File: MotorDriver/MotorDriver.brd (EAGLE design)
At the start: 50 x 50 mm, 85 parts, among them IC1 DRV8320RSRHAR, IC2 MAX3051ESA+, IC3 TPD4S014DSQR, J1 J_USB_MICROAB_HIROSE_ZX62-AB-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, J2 SM03B-ZESS-TB, Q1 BUK7Y7R8-80EX, Q2 BUK7Y7R8-80EX, Q3 BUK7Y7R8-80EX, Q4 BUK7Y7R8-80EX, Q5 BUK7Y7R8-80EX, Q6 BUK7Y7R8-80EX, U1 LPC1549JBD48, U2 ADCMP350YKSZ, U3 MCP1700T-33, U4 ADR5041, Y1 FA238V

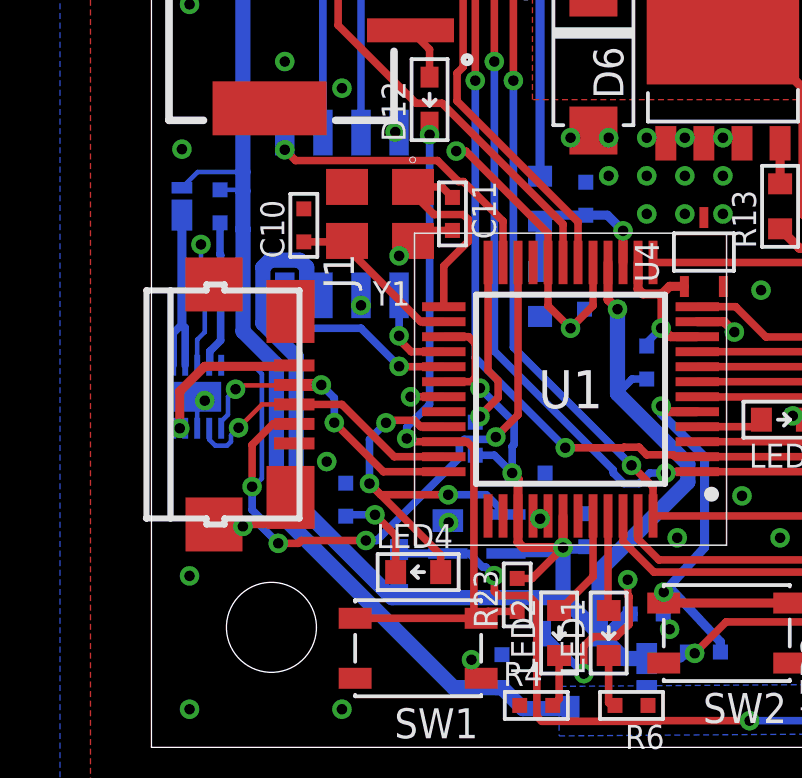
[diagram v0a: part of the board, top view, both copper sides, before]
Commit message: デバイス側で`id`を使ってUSBの接続を検出するのは不可能なので保護ICの`!ack`を使うように変更
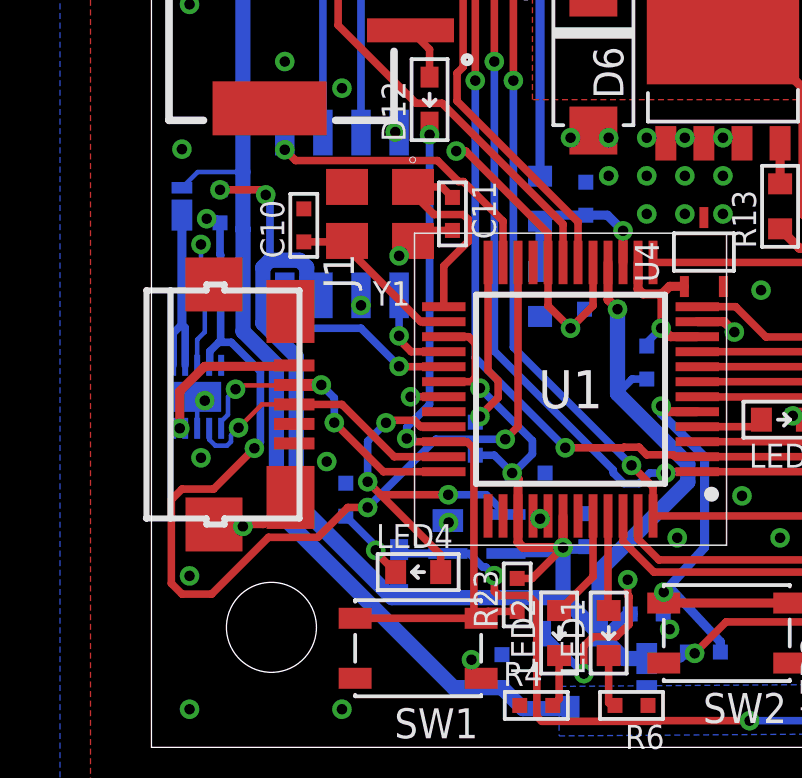
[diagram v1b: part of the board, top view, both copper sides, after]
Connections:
- removed net ID: IC3.5, J1.P$4, U1.22
- removed net N$29: IC3.4, R12.1
- new net !USB_ACK: IC3.4, R12.1, U1.22
- net +3V3: now also R12.2
- net +5V: no longer R12.2
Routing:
- net !USB_ACK: track 0.00 -> 35.6 mm, vias 0 -> 4
- net ID: track 25.9 -> 0.00 mm, vias 4 -> 0
- net N$29: track 4.92 -> 0.00 mm
- net +3V3: track 69.4 -> 73.8 mm, vias 5 -> 7
- net +5V: track 91.0 -> 90.3 mm
- net N$27: track 3.19 -> 2.55 mm
- net GND: vias 78 -> 79

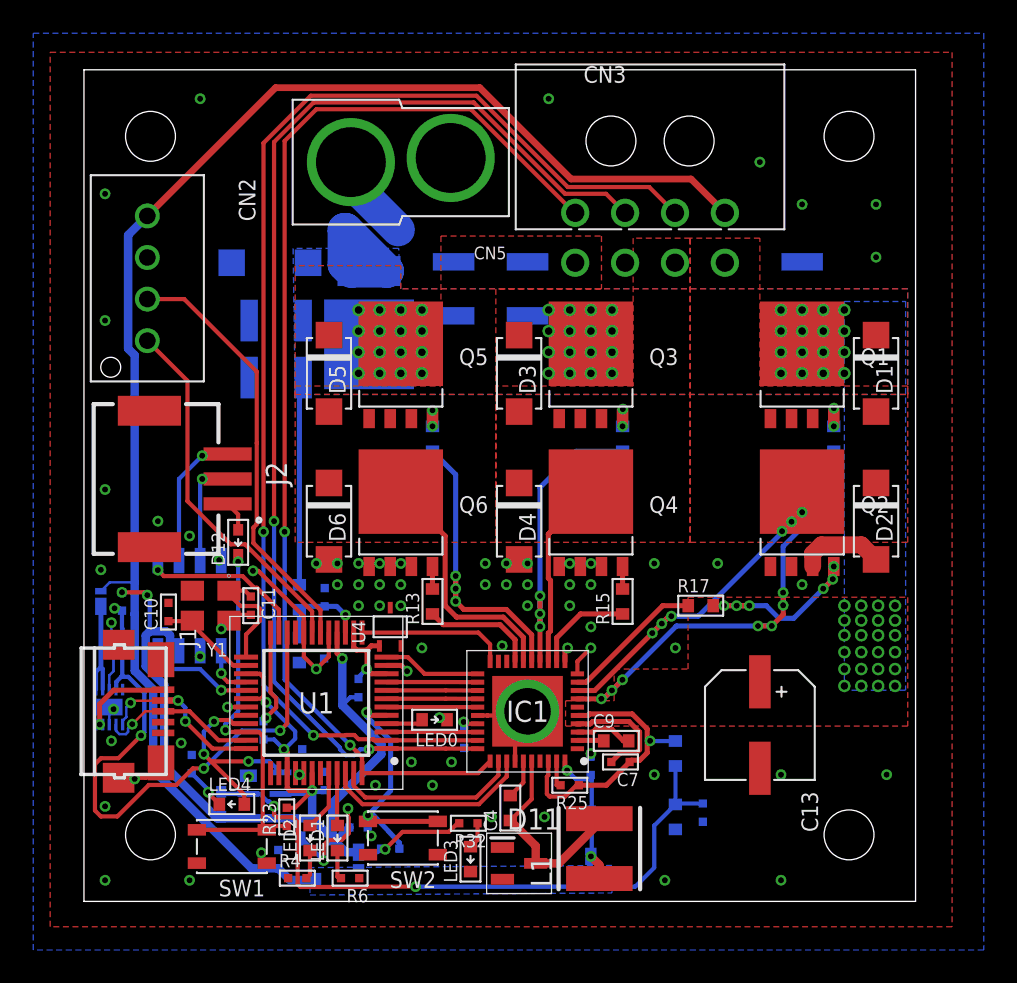
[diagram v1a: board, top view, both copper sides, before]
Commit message: [fix]USB-ACKのプルアップ抵抗の変更とコメントの整理
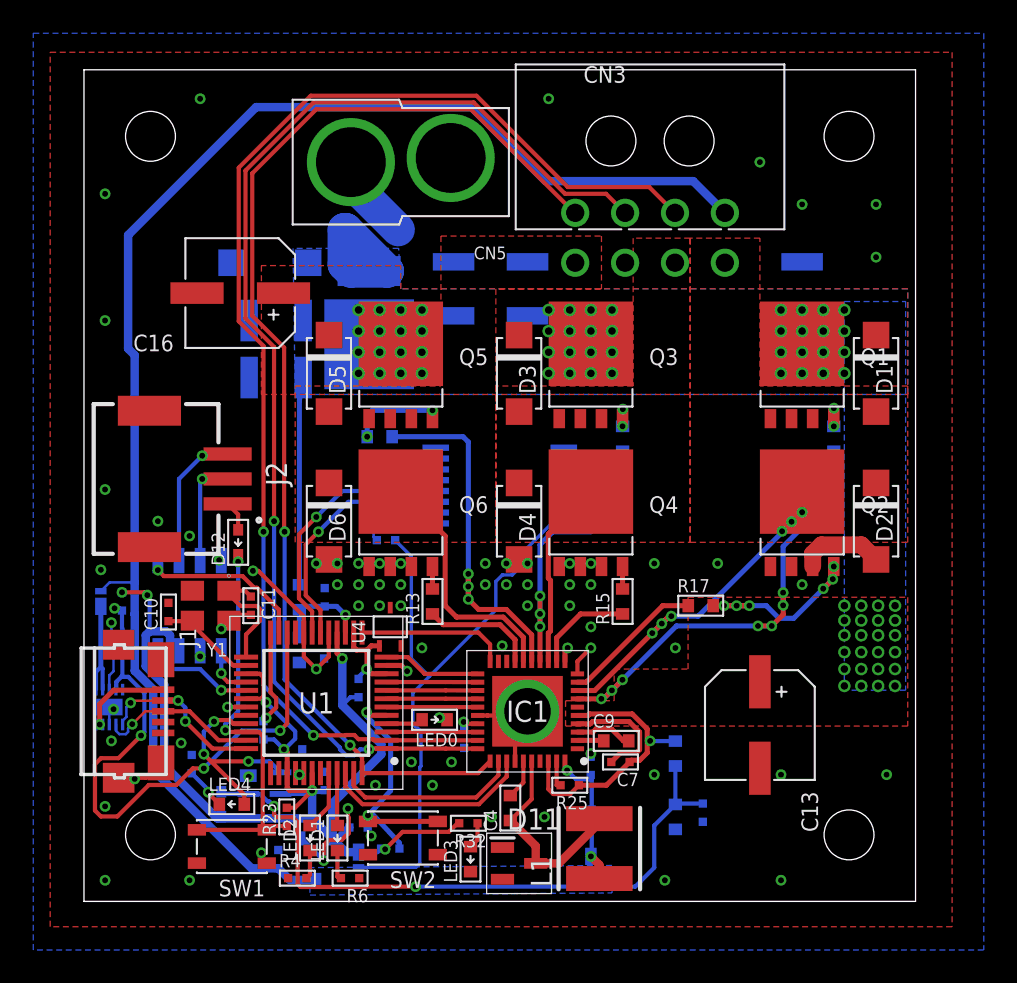
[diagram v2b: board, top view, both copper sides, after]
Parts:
- removed CN2: (no value), con-Molex:53375-04
- added C15: 0.1u, MotorDriver:C1005
- added C16: 22u, Passive:ES-6.3
- added LED5: RED, MotorDriver:LED1608
- added R8: 4.7k, MotorDriver:R1005
- added U5: AS5145B, ic-ams:SSOP16
- D10: value SMAJ60A -> SMAJ54A
- F1: value 15 -> 20
- LED0, LED3: value (none) -> RED
- LED1: value (none) -> GREEN
- LED2: value (none) -> WHITE
- R12: value 2.2k -> 10k
- R18: value (none) -> 10k
- moved R3 3.18 mm to (17.8, 27.9), turned to 0 degrees
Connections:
- new net N$29: C15.1, U5.15
- new net N$30: LED5.K, U5.1, U5.2
- new net N$32: LED5.A, R8.1
- net +5V: now also R8.2, U5.16; no longer CN2.4
- net GND: now also C15.2, C16.N, U5.10, U5.11, U5.7, U5.8; no longer CN2.3
- net QEI_A: now also U5.3; no longer CN2.2
- net QEI_B: now also U5.4; no longer CN2.1
- net V+: now also C16.P
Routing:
- net +5V: track 90.3 -> 127.4 mm
- net QEI_A: track 25.8 -> 14.5 mm, vias 0 -> 1
- net QEI_B: track 22.2 -> 15.5 mm, vias 0 -> 1
- net N$13: track 1.47 -> 5.84 mm
- net GH_C: track 18.1 -> 22.0 mm
- net N$29: track 0.00 -> 3.07 mm
- net N$30: track 0.00 -> 3.00 mm
- net HALL_W: track 68.8 -> 70.4 mm
- net HALL_V: track 71.6 -> 73.0 mm
- net N$32: track 0.00 -> 1.35 mm
- net HALL_U: track 75.7 -> 76.9 mm

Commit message: [fix]仕様確定に伴って変更
*電源電圧を24[V]に
*エンコーダICが廃盤になったので変更
*電源強化
*部品票の更新
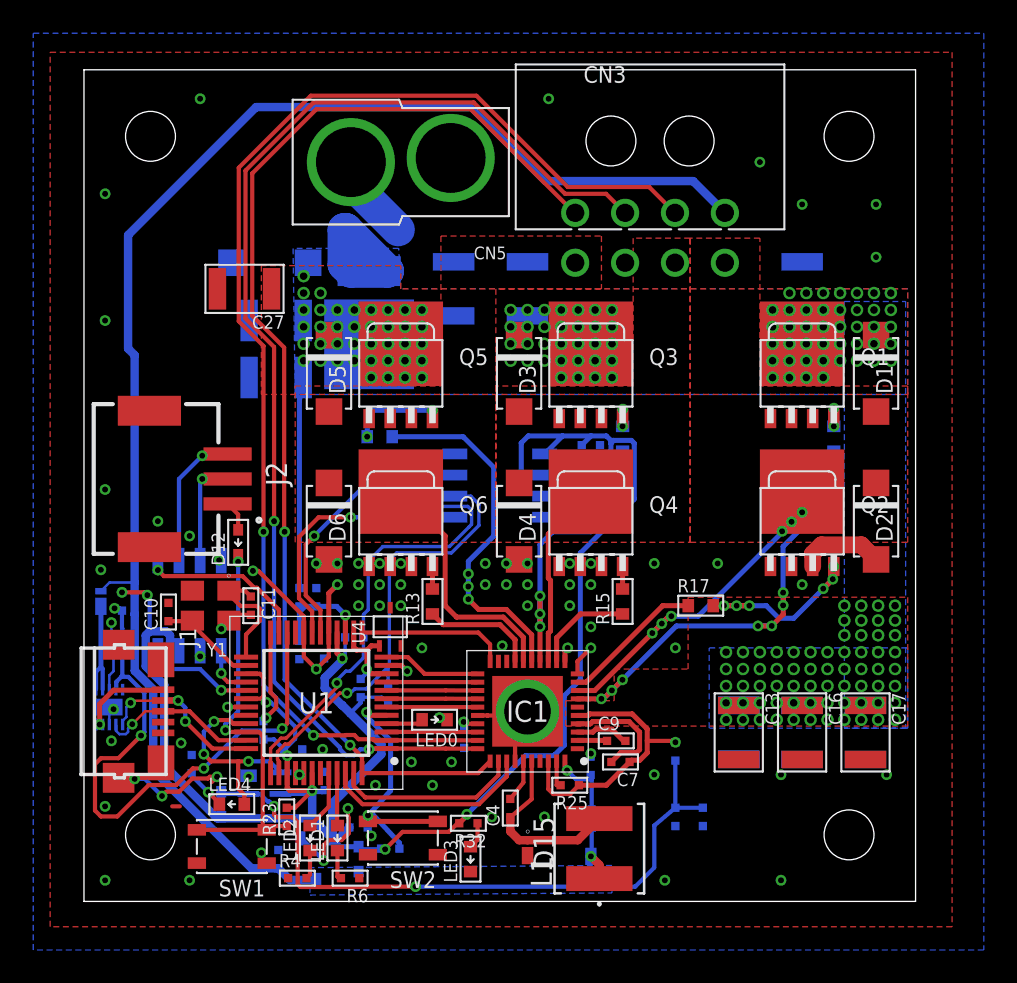
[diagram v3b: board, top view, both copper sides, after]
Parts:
- removed D11: HSMS-2800-TR1G, HSMS-2800-TR1G:SOT96P240X120-3N
- removed LED5: RED, MotorDriver:LED1608
- removed R8: 4.7k, MotorDriver:R1005
- removed U5: AS5145B, ic-ams:SSOP16
- added C17, C18, C21, C25, C26, C27: 10u, MotorDriver:C3225
- added C28: 0.1u, MotorDriver:C1005
- added D15: SDM2U40CSP-7B, SDM2U40CSP-7B:X3-WLB1608-2
- added IC5: AS5601-ASOM, AS5601-ASOM:SOIC127P600X175-8N
- added R19, R24: 2.2k, MotorDriver:R1005
- C1, C2, C3: value 10u -> 22u
- C13, C16: value 22u -> 10u; device Passive:ES-6.3 -> MotorDriver:C3225
- C14, C5: value 0.47u -> 47n
- C4, C9: device MotorDriver:C1608 -> MotorDriver:C1005
- CN3: device con-Molex:43045-0800 -> MotorDriver:43045-0800
- D1, D2, D3, D4, D5, D6: value NRVTSA4100ET3G -> SK34ATR
- D10: value SMAJ54A -> SMAJP4KE30A
- D13: device Diode:SMPC -> diode:SMPC
- D7: value SDM2U40CSP-7B -> (none); device SDM2U40CSP-7B:X3-WLB1608-2 -> MotorDriver:DIODE_SOD523
- L1: value NR5040T330M -> NR5040T2R2N; device NR5040T330M:NR5040T2R2N -> nr5040:IND_TAIYO_NR5040
- LED4: value (none) -> RED
- Q1, Q2, Q3, Q4, Q5, Q6: value BUK7Y7R8-80EX -> BUK7Y3R5-40E; device MotorDriver:SOT669 -> NXP_60_26022015:SOT669
- R10, R22, R9: device MotorDriver:R1608 -> MotorDriver:R1005
- R20: value 47k -> 22k; device MotorDriver:R1608 -> MotorDriver:R1005
- moved C16 42.9 mm to (43.2, 10.2), turned to 270 degrees
- moved C13 1.35 mm to (39.4, 10.2)
- moved C5 0.51 mm to (14.0, 18.3)
- moved C15 0.36 mm to (30.5, 25.7), turned to 0 degrees
- moved C14 0.25 mm to (37.2, 5.08)
- moved D7 0.13 mm to (16.5, 2.54)
- moved R21 0.13 mm to (16.6, 12.8)
- moved R9 0.13 mm to (35.6, 9.02)
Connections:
- removed net N$29: C15.1, U5.15
- removed net N$30: LED5.K, U5.1, U5.2
- removed net N$32: LED5.A, R8.1
- new net SCL: IC5.7, R19.1, U1.37
- new net SDA: IC5.6, R24.1, U1.38
- net +3V3: now also C15.1, C28.1, D7.A, IC5.1, IC5.2, R19.2, R24.2; no longer D7.2
- net +5V: now also D7.K; no longer D7.1, R8.2, U5.16
- net GND: now also C13.2, C16.2, C17.2, C18.2, C21.2, C25.2, C26.2, C27.2, C28.2, D15.2, IC5.4; no longer C13.N, C16.N, D11.1, U5.10, U5.11, U5.7, U5.8
- net N$3: now also D15.1; no longer D11.3
- net QEI_A: now also IC5.8; no longer U5.3
- net QEI_B: now also IC5.5; no longer U5.4
- net V+: now also C13.1, C16.1, C17.1, C18.1, C21.1, C25.1, C26.1, C27.1; no longer C13.P, C16.P
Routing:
- net +3V3: track 73.8 -> 121.3 mm, vias 7 -> 8
- net +5V: track 127.4 -> 89.3 mm
- net SCL: track 0.00 -> 28.3 mm, vias 0 -> 1
- net SDA: track 0.00 -> 26.8 mm, vias 0 -> 1
- net GND: track 39.4 -> 49.3 mm, vias 79 -> 82
- net N$29: track 3.07 -> 0.00 mm
- net N$30: track 3.00 -> 0.00 mm
- net QEI_A: track 14.5 -> 16.9 mm
- net N$32: track 1.35 -> 0.00 mm
- net N$3: track 12.5 -> 11.2 mm
- net FUSE: track 12.7 -> 12.1 mm
- net V+: track 29.0 -> 29.2 mm, vias 73 -> 182

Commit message: tmpからもってきた
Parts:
- removed D14: RB520S, MotorDriver:DIODE_SOD523
- removed D15: SDM2U40CSP-7B, SDM2U40CSP-7B:X3-WLB1608-2
- removed IC1: DRV8320RSRHAR, DRV8320RSRHAR:QFN50P600X600X100-41N
- removed LED4: RED, MotorDriver:LED1608
- removed R10: 2.2k, MotorDriver:R1005
- removed R11: 330, MotorDriver:R1005
- removed R9: 33k, MotorDriver:R1005
- removed U2: ADCMP350YKSZ, adcmp350:KS_4
- added C29, C31: 1u, MotorDriver:C1005
- added C30: 47n, MotorDriver:C1005
- added IC4: DRV8320SRTVT, DRV8320SRTVT:QFN50P500X500X80-33N
- added IC6: LM5160QPWPRQ1, LM5160QPWPRQ1:SOP65P640X110-15N
- added R27: 2.2k, MotorDriver:R1005
- added R28: 2.2, MotorDriver:R1005
- added R8: 51k, MotorDriver:R1005
- C14: value 47n -> 10u; device MotorDriver:C1005 -> MotorDriver:C3225
- C4: value 0.1u -> 10n
- C7: value 1u -> 0.1u
- C8: value 1u -> 4.7u; device MotorDriver:C1005 -> Passive:1608
- C9: value 47n -> 22n
- L1: value NR5040T2R2N -> 15u; device nr5040:IND_TAIYO_NR5040 -> Passive:L4949
- R1: value 12k -> 120k
- R2: value 2.2k -> 10k
- R25: value 100k -> 3.3k
- moved R1 43.8 mm to (9.02, 43.2)
- moved C9 39.5 mm to (7.75, 40.8), flipped to the bottom, turned to 90 degrees
- moved R2 39.0 mm to (9.02, 40.8)
- moved L1 37.7 mm to (3.68, 29.2), flipped to the bottom, turned to 270 degrees
- moved C7 35.3 mm to (7.62, 33.7), flipped to the bottom, turned to 270 degrees
- moved D8 34.6 mm to (3.68, 24.3), turned to 180 degrees
- moved R25 31.9 mm to (8.38, 31.1), flipped to the bottom, turned to 90 degrees
- moved C4 31.5 mm to (7.11, 31.1), flipped to the bottom
- moved C8 23.5 mm to (2.03, 20.6), turned to 90 degrees
- moved C14 5.27 mm to (35.8, 10.2), flipped to the top, turned to 270 degrees
- moved C18 3.56 mm to (35.8, 10.2)
- moved U4 0.57 mm to (18.7, 17.0)
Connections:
- removed net FUSE: LED4.A, U1.33, U2.3
- removed net N$20: IC1.39, R25.2
- removed net N$25: C14.2, D14.A, R10.2, R9.1, U2.1
- removed net N$27: LED4.K, R11.2
- new net N$32: C31.1, IC4.24
- new net N$48: C30.1, IC4.32
- new net N$55: C29.2, IC4.2
- new net N$56: C30.2, IC4.1
- new net VBAT/2: CN5.P, F1.2, IC6.3, R1.2, R8.1
- net !BRAKE: now also IC4.30; no longer IC1.33
- net !CS: now also IC4.21; no longer IC1.24
- net !FAULT: now also IC4.17; no longer IC1.20
- net +3V3: no longer D14.K, U2.4
- net DIR: now also IC4.29; no longer IC1.32
- net GH_A: now also IC4.5; no longer IC1.7
- net GH_B: now also IC4.12; no longer IC1.14
- net GH_C: now also IC4.13; no longer IC1.15
- net GL_A: now also IC4.7; no longer IC1.9
- net GL_B: now also IC4.10; no longer IC1.12
- net GL_C: now also IC4.15; no longer IC1.17
- net GND: now also C14.2, C31.2, C7.1, C8.1, C9.1, IC4.16, IC4.23, IC4.31, IC4.33, IC4.8, IC4.9, IC6.1, IC6.15, IC6.2, R2.1, R27.2; no longer C14.1, C8.2, D15.2, IC1.1, IC1.10, IC1.11, IC1.18, IC1.19, IC1.26, IC1.34, IC1.41, R10.1, R11.1, R2.2, U2.2
- net HALL_U: now also IC4.26; no longer IC1.29
- net HALL_V: now also IC4.27; no longer IC1.30
- net HALL_W: now also IC4.28; no longer IC1.31
- net N$1: now also C7.2, IC6.10, IC6.8; no longer IC1.40, R1.2, R2.1
- net N$16: now also C4.1, IC6.12, IC6.13, L1.1; no longer C7.2, IC1.4
- net N$17: now also IC6.9, R25.2, R27.1; no longer C8.1, IC1.27
- net N$18: now also C4.2, IC6.11; no longer C9.1, IC1.2
- net N$19: now also C8.2, R28.2; no longer C9.2, IC1.3
- net N$2: now also IC6.5, R8.2; no longer D8.2, L1.1, R1.1
- net N$26: now also D8.2, L1.2, R25.1, R28.1; no longer CN5.P, F1.2
- net N$3: now also IC6.4, R1.1, R2.2; no longer C4.1, D15.1, IC1.36, L1.2
- net N$4: now also C9.2, IC6.6; no longer C4.2, IC1.35
- net PWM_AH: now also IC4.25; no longer IC1.28
- net PWM_EN: now also IC4.22; no longer IC1.25
- net SCLK: now also IC4.20; no longer IC1.23
- net SDI: now also IC4.19; no longer IC1.22
- net SDO: now also IC4.18; no longer IC1.21
- net SH_A: now also IC4.6; no longer IC1.8
- net SH_B: now also IC4.11; no longer IC1.13
- net SH_C: now also IC4.14; no longer IC1.16
- net V+: now also C14.1, C29.1, IC4.3, IC4.4; no longer C7.1, IC1.38, IC1.5, IC1.6, R25.1, R9.2
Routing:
- net N$25: track 41.7 -> 0.00 mm, vias 2 -> 0
- net VBAT/2: track 0.00 -> 22.0 mm
- net V+: track 29.2 -> 12.7 mm, vias 182 -> 167
- net +5V: track 89.3 -> 102.7 mm
- net FUSE: track 12.1 -> 0.00 mm, vias 3 -> 0
- net SH_B: track 15.0 -> 7.32 mm
- net N$17: track 1.36 -> 8.27 mm, vias 1 -> 0
- net N$48: track 0.00 -> 4.20 mm
- net HALL_V: track 73.0 -> 76.8 mm
- net N$26: track 5.24 -> 8.83 mm
- net HALL_W: track 70.4 -> 73.8 mm
- net N$16: track 7.12 -> 3.74 mm
- net GND: track 49.3 -> 45.9 mm, vias 82 -> 79
- net N$18: track 1.79 -> 4.98 mm
- net HALL_U: track 76.9 -> 80.1 mm
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- added copper zone on layer 16, net N$16
- added copper zone on layer 16, net N$26
- removed copper zone on layer 16, net +5V
